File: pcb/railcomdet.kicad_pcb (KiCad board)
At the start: 4 copper layers, 110 x 70 mm, 162 parts, among them J1 MVE252-5-V, J10 MVE252-5-V, J2 MVE252-5-V, J3 MVE252-5-V, J4 MVE252-5-V, J5 MVE252-5-V, J6 PINHEADER, J7 PINHEADER, J8 PROG/DEBUG, J9 MVE252-5-V, SW1 6x6, U1 VO0631T, U10 LM339, U11 LM339, U12 STM32F103C8Tx, U13 AMS1117-3.3, U14 L78L05_SOT89, U15 SN75176AP, U2 VO0631T, U3 VO0631T, U4 L78L05_SOT89, U5 L79L05_SOT89, U6 LM339, U7 LM339, U8 LM339, U9 4052, Y1 14,7456MHz

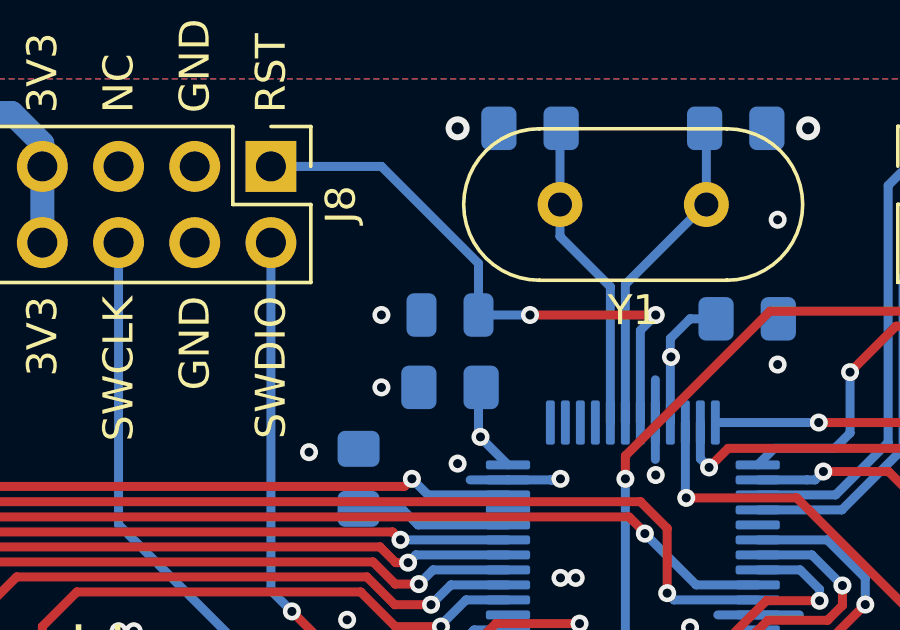
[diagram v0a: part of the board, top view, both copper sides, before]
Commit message: pcb: silkscreen.
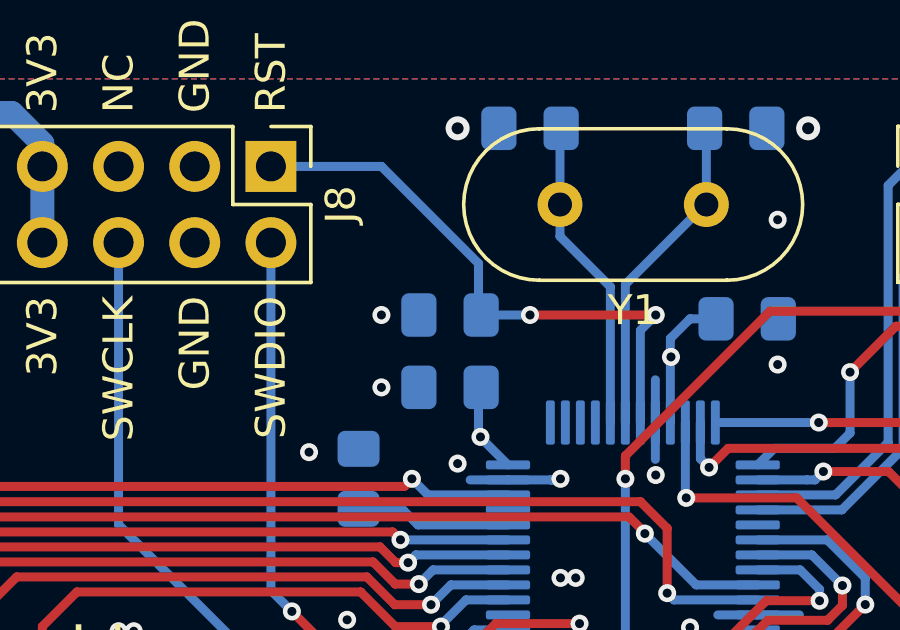
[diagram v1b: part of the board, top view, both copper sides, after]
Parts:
- C21: footprint Capacitor_SMD:C_0805_2012Metric -> Capacitor_SMD:C_0805_2012Metric_Pad1.18x1.45mm_HandSolder

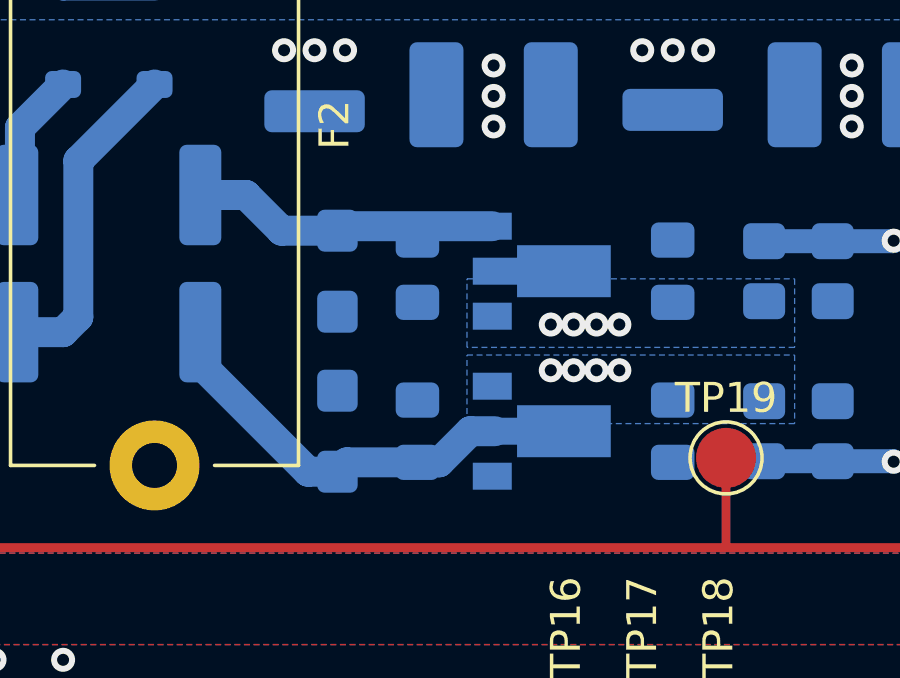
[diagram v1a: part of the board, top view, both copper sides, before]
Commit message: Use SOT83-handsolder for DCC part.
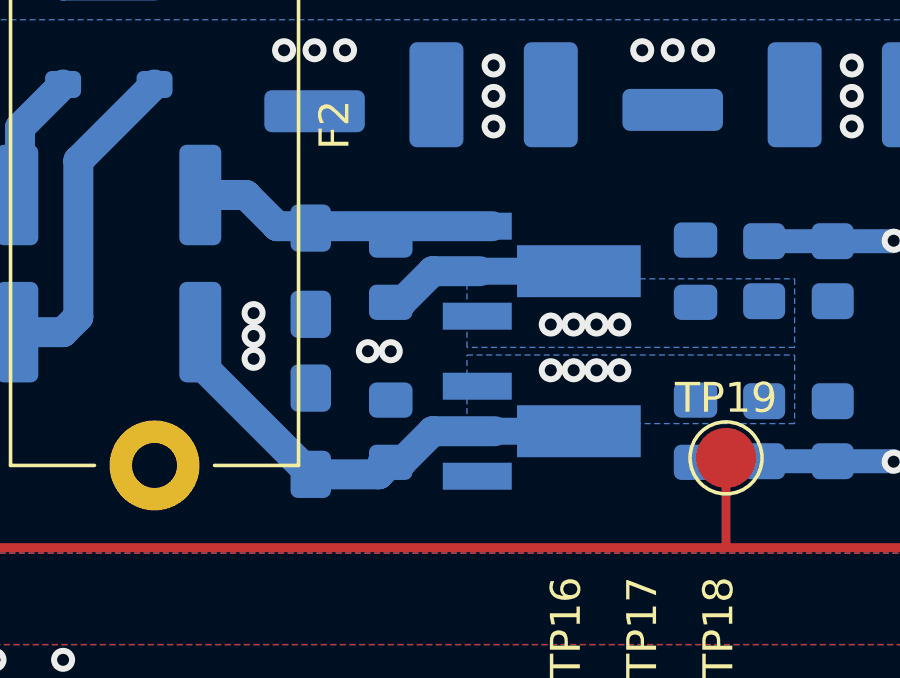
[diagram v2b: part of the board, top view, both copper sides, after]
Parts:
- C5, C6: footprint Capacitor_Tantalum_SMD:CP_EIA-3216-10_Kemet-I -> Capacitor_Tantalum_SMD:CP_EIA-3216-10_Kemet-I_Pad1.58x1.35mm_HandSolder
- U4, U5: footprint Package_TO_SOT_SMD:SOT-89-3 -> Package_TO_SOT_SMD:SOT-89-3_Handsoldering
- moved C5 0.89 mm to (112.6, 56.6)
- moved C6 0.89 mm to (112.6, 62.0)
- moved C7 0.89 mm to (115.3, 56.6)
- moved C8 0.89 mm to (115.3, 62.0)
- moved C10 0.76 mm to (125.5, 62.0)
- moved C9 0.76 mm to (125.5, 56.6)
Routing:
- net GNDA: track 0.00 -> 3.40 mm, vias 55 -> 60

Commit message: Pcb tweaks.
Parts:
- added REF**: OSHW-Logo_11.4x12mm_SilkScreen, Symbol:OSHW-Logo_11.4x12mm_SilkScreen, F.Cu at (196.6, 49.0)
- D3: value Yellow -> WHITE
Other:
- board text added: "Kateřina Hanáková, Jan Horáček LRKV MENDELU, KMŽ Brno I 2023-2024"
- board text added: "MTB-RC v1.0 MTBbus RailCom detector"
- board text added: "MU1 MU2"
- board text added: "RX2 RX1"
- board text added: "TEST"

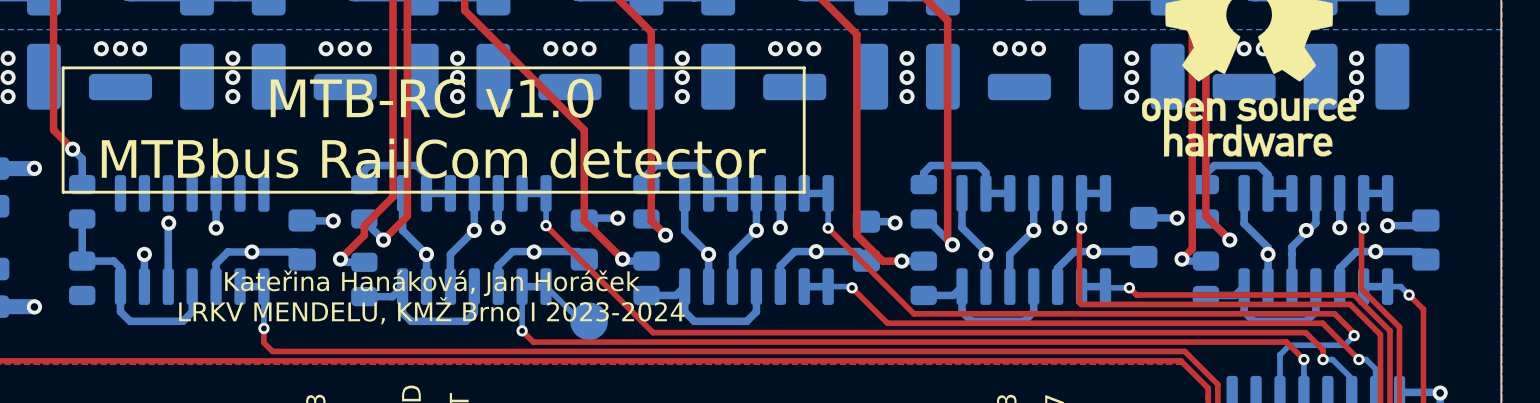
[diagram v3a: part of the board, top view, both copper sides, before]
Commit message: Wire empty inputs of U11.
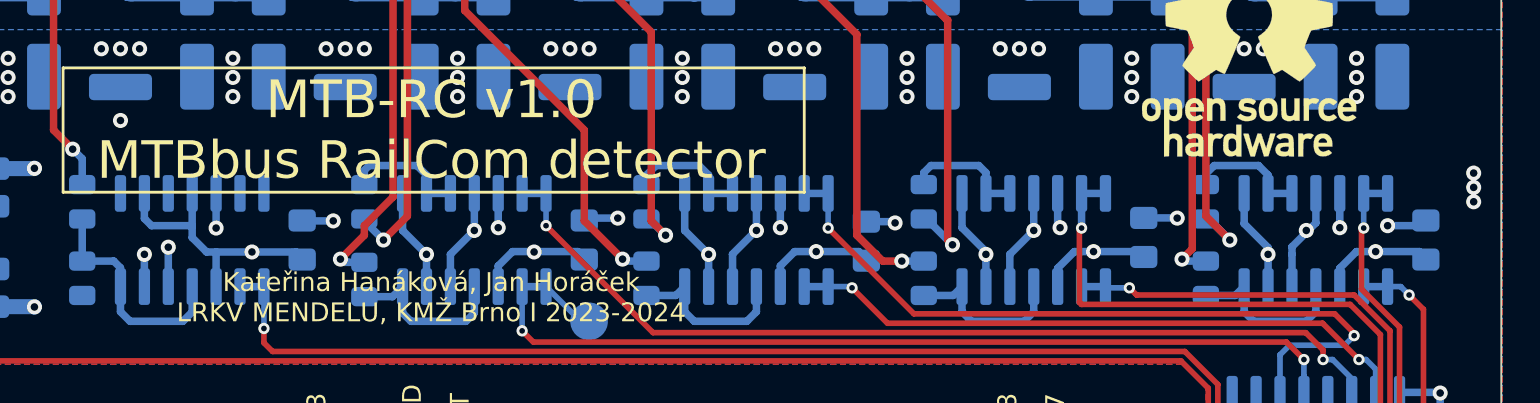
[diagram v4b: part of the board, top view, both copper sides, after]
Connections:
- U11 pad 10: unconnected-(U11C---Pad10) -> GNDA
- U11 pad 11: unconnected-(U11C-+-Pad11) -> +5VA
- U11 pad 8: unconnected-(U11D---Pad8) -> GNDA
- U11 pad 9: unconnected-(U11D-+-Pad9) -> +5VA
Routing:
- net +5VA: track 50.0 -> 58.3 mm
- net GNDA: vias 60 -> 64

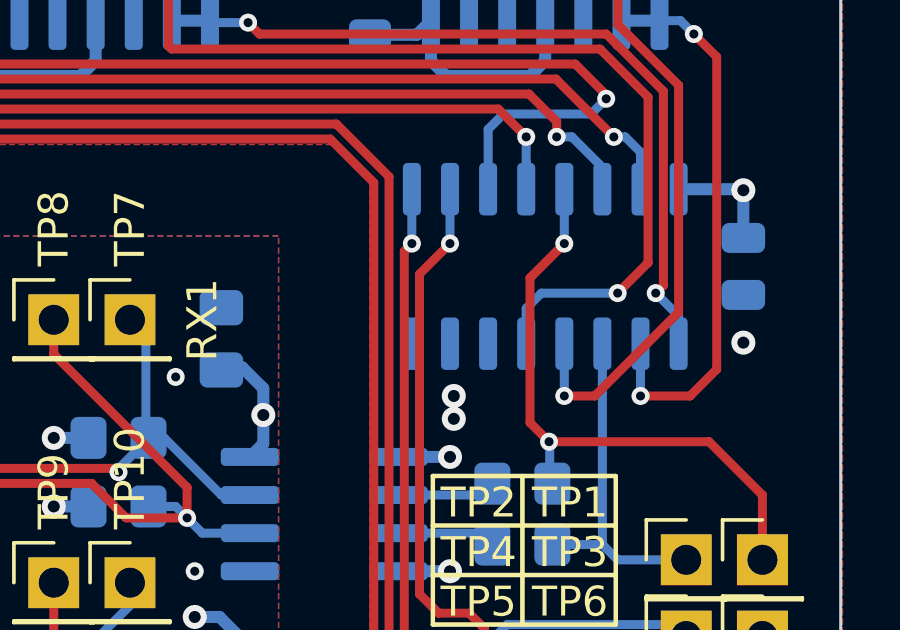
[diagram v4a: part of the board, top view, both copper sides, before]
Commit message: VEE of 4052 to -5VA.
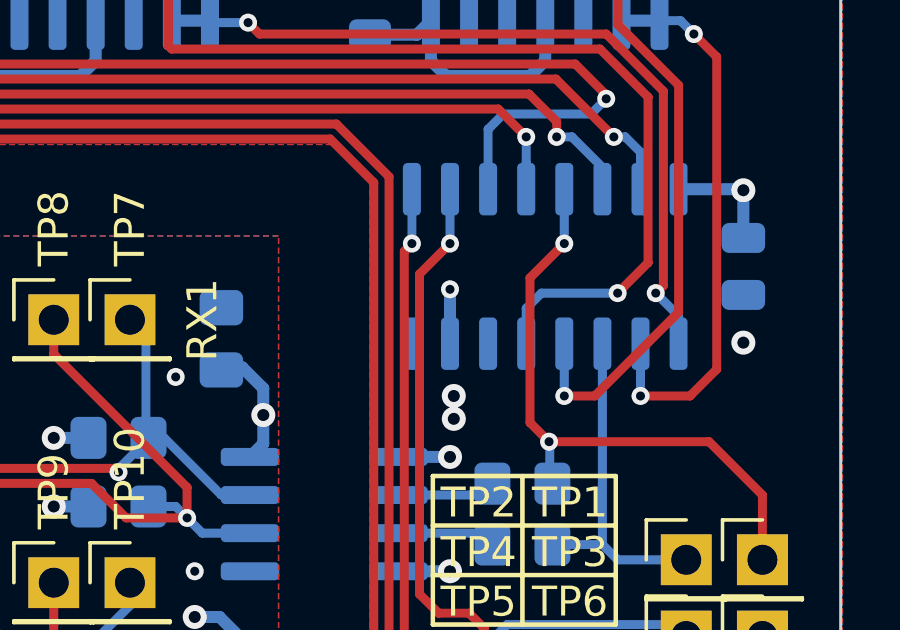
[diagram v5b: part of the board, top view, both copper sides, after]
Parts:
- R11, R7: value 10k -> 2k2
- R3: value 1k -> 1k5
- R8, R9: value 1k -> 220R
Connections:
- U9 pad 7: GNDA -> -5VA
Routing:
- net -5VA: track 18.1 -> 32.7 mm, vias 14 -> 15
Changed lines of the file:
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@@
         (effects (font (size 1 1) (thickness 0.15)) (justify mirror))
     )
-    (fp_text value "1k" (at 0 -1.65 180) (layer "B.Fab")
+    (fp_text value "220R" (at 0 -1.65 180) (layer "B.Fab")
         (effects (font (size 1 1) (thickness 0.15)) (justify mirror))
     )
@@
       (net 5 "GNDA") (pinfunction "Inh") (pintype "input"))
     (pad "7" smd roundrect (at -2.575 -3.175 90) (size 1.75 0.6) (layers "B.Cu" "B.Paste" "B.Mask") (roundrect_rratio 0.25)
-      (net 5 "GNDA") (pinfunction "VEE") (pintype "power_in"))
+      (net 8 "-5VA") (pinfunction "VEE") (pintype "power_in"))
     (pad "8" smd roundrect (at -2.575 -4.445 90) (size 1.75 0.6) (layers "B.Cu" "B.Paste" "B.Mask") (roundrect_rratio 0.25)
       (net 5 "GNDA") (pinfunction "VSS") (pintype "power_in"))
@@
         (effects (font (size 1 1) (thickness 0.15)) (justify mirror))
     )
-    (fp_text value "10k" (at 0 -1.65 180) (layer "B.Fab")
+    (fp_text value "2k2" (at 0 -1.65 180) (layer "B.Fab")
         (effects (font (size 1 1) (thickness 0.15)) (justify mirror))
     )
@@
         (effects (font (size 1 1) (thickness 0.15)) (justify mirror))
     )
-    (fp_text value "1k" (at 0 -1.65 180) (layer "B.Fab")
+    (fp_text value "220R" (at 0 -1.65 180) (layer "B.Fab")
         (effects (font (size 1 1) (thickness 0.15)) (justify mirror))
     )
@@
         (effects (font (size 1 1) (thickness 0.15)) (justify mirror))
     )
-    (fp_text value "1k" (at 0 -1.65) (layer "B.Fab")
+    (fp_text value "1k5" (at 0 -1.65) (layer "B.Fab")
         (effects (font (size 1 1) (thickness 0.15)) (justify mirror))
     )
@@
         (effects (font (size 1 1) (thickness 0.15)) (justify mirror))
     )
-    (fp_text value "10k" (at 0 -1.65 180) (layer "B.Fab")
+    (fp_text value "2k2" (at 0 -1.65 180) (layer "B.Fab")
         (effects (font (size 1 1) (thickness 0.15)) (justify mirror))
     )
@@
   (via (at 121.412 59.944) (size 0.8) (drill 0.4) (layers "F.Cu" "B.Cu") (free) (net 8))
   (via (at 147.955 58.42) (size 0.8) (drill 0.4) (layers "F.Cu" "B.Cu") (free) (net 8))
+  (via (at 196.977 70.866) (size 0.6) (drill 0.3) (layers "F.Cu" "B.Cu") (net 8))
   (via (at 177.8 58.527091) (size 0.8) (drill 0.4) (layers "F.Cu" "B.Cu") (free) (net 8))
   (via (at 120.65 59.944) (size 0.8) (drill 0.4) (layers "F.Cu" "B.Cu") (free) (net 8))
@@
   (via (at 192.786 58.273091) (size 0.8) (drill 0.4) (layers "F.Cu" "B.Cu") (free) (net 8))
   (via (at 171.704 58.781091) (size 0.8) (drill 0.4) (layers "F.Cu" "B.Cu") (free) (net 8))
+  (segment (start 194.691 66.6115) (end 194.691 70.231) (width 0.8) (layer "In2.Cu") (net 8))
+  (segment (start 199.3265 61.976) (end 194.691 66.6115) (width 0.8) (layer "In2.Cu") (net 8))
+  (segment (start 194.691 70.231) (end 195.326 70.866) (width 0.8) (layer "In2.Cu") (net 8))
+  (segment (start 195.326 70.866) (end 196.977 70.866) (width 0.8) (layer "In2.Cu") (net 8))
+  (segment (start 196.977 72.679) (end 196.977 70.866) (width 0.4) (layer "B.Cu") (net 8))
   (segment (start 201.422 56.961) (end 201.422 58.781091) (width 0.4) (layer "B.Cu") (net 8))
   (segment (start 186.436 58.654091) (end 186.563 58.781091) (width 0.4) (layer "B.Cu") (net 8))
